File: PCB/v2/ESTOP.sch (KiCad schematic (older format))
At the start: 6 parts, among them J7 ESTOP_SOFT, Q2 Q_PMOS_GSD, Q5 2N7002

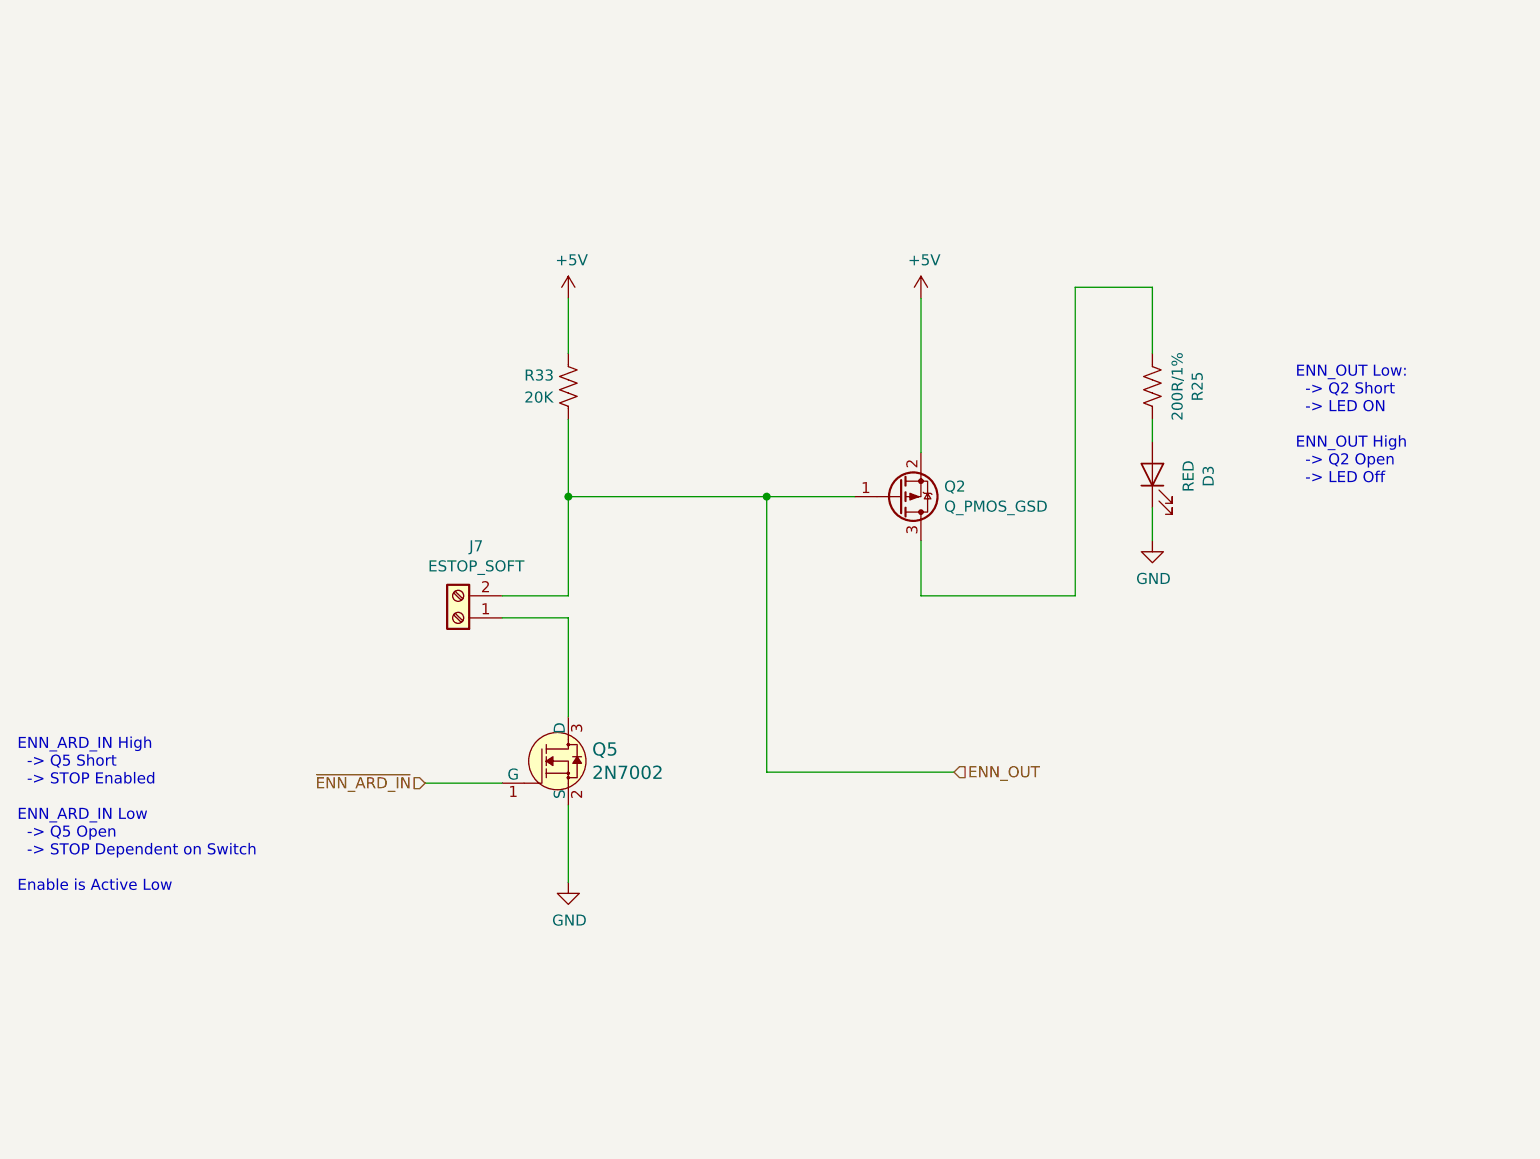
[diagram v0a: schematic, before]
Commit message: Add 12V to ENN Loop
Added 12v detection to ENN loop, so EN on tmc would be high if 12v not present but 5v is.
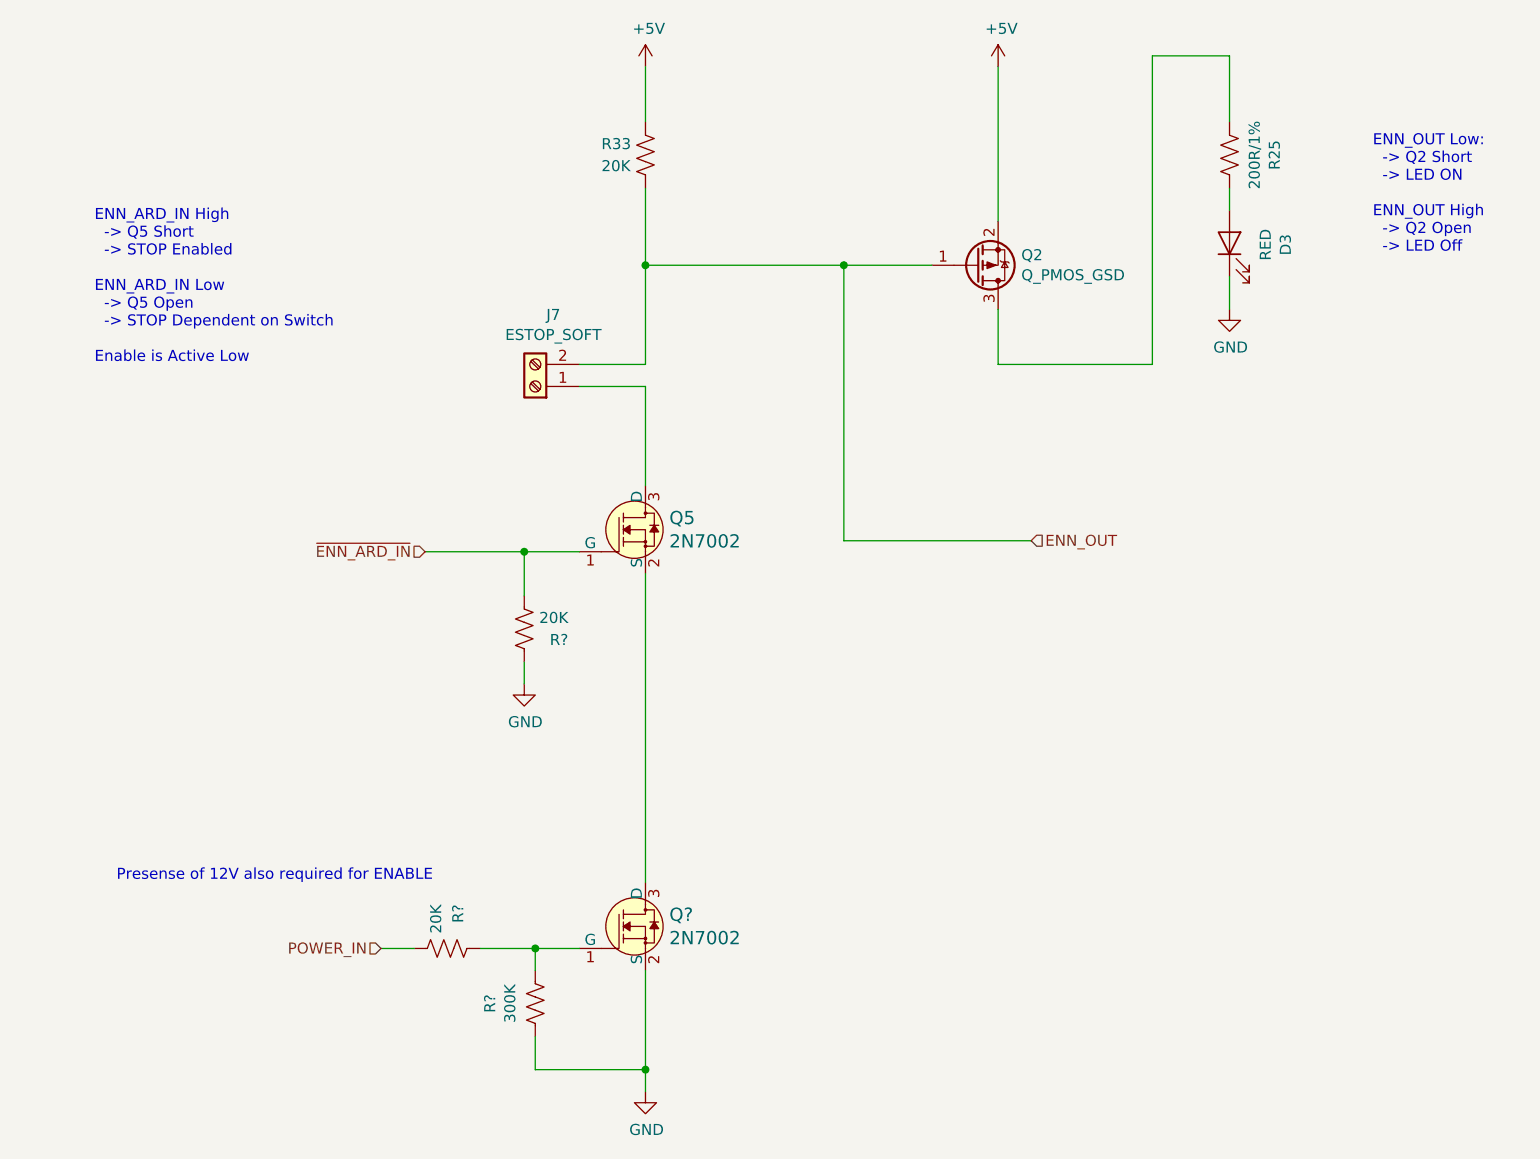
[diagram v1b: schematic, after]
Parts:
- added Q?: 2N7002, digikey-footprints:SOT-23-3, symbol dk_Transistors-FETs-MOSFETs-Single:2N7002
- added R? (x2): 20K, Resistor_SMD:R_0603_1608Metric, symbol MMTK-rescue:R_US-Device-MMTK-rescue-MMTK-rescue
- added R?: 300K, Resistor_SMD:R_0603_1608Metric, symbol MMTK-rescue:R_US-Device-MMTK-rescue-MMTK-rescue
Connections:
- net GND: now also Q?.2 (S), R?.2, R?.2; no longer Q5.2 (S)
- net ~ENN_ARD_IN: now also R?.1
- new net: Q5.2 (S), Q?.3 (D)
- new net: Q?.1 (G), R?.1, R?.2
- new net POWER_IN: R?.1
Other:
- note added: "Presense of 12V also required for ENABLE"
- moved on the sheet: D3, J7, Q2, Q5, R25, R33
